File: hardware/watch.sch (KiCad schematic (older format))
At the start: 42 parts, among them J1 Conn_01x04_Male, J2 Conn_01x04_Male, SW1 SW_Push, SW2 SW_Push, U1 KCSA02-105, U10 STP08DP05, U11 KCSA02-105, U12 STP08DP05, U13 KCSA02-105, U2 KCSA02-105, U3 STP08DP05, U4 STP08DP05, U5 STM32L011F4Px, U6 TLV70033_SOT23-5, U7 MCP73831-2-OT, U8 LM66100, U9 LM66100, Y1 32kHz

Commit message: updated firmware
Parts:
- removed J1, J2: Conn_01x04_Male, watch:CONN_1x4_SMD, symbol Connector:Conn_01x04_Male
- added J1: Conn_01x02_Male, Connector_PinHeader_2.54mm:PinHeader_1x02_P2.54mm_Vertical, symbol Connector:Conn_01x02_Male
- added J2, J4: Conn_01x03_Male, Connector_PinHeader_2.54mm:PinHeader_1x03_P2.54mm_Vertical, symbol Connector:Conn_01x03_Male
- added J3, J5: Conn_01x01_Male, Connector_PinHeader_2.54mm:PinHeader_1x01_P2.54mm_Vertical, symbol Connector:Conn_01x01_Male
- BT1: footprint watch:BAT_PAD -> Connector_PinHeader_2.54mm:PinHeader_1x02_P2.54mm_Vertical
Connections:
- wire segments 134 -> 138
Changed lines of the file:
@@
 Title "Armbanduhr"
 Date "2020-09-20"
-Rev "1"
+Rev "2"
 Comp "Probieren geht über studieren. Immer."
 Comment1 "Andreas Kohler"
@@
 F 0 "BT1" H 2418 6146 50  0000 L CNN
 F 1 "Battery_Cell" H 2418 6055 50  0000 L CNN
-F 2 "watch:BAT_PAD" V 2300 6110 50  0001 C CNN
+F 2 "Connector_PinHeader_2.54mm:PinHeader_1x02_P2.54mm_Vertical" V 2300 6110 50  0001 C CNN
 F 3 "~" V 2300 6110 50  0001 C CNN
 F 4 "https://www.amazon.de/Turnigy-nano-tech-300mah-Solo-Pro-Modellbau/dp/B016339JKO/" H 2300 6050 50  0001 C CNN "Order"
@@
 	1    0    0    -1
 $EndComp
-$Comp
-L Connector:Conn_01x04_Male J1
-U 1 1 5F717493
-P 4300 950
-F 0 "J1" H 4408 1231 50  0000 C CNN
-F 1 "Conn_01x04_Male" H 4408 1140 50  0000 C CNN
-F 2 "watch:CONN_1x4_SMD" H 4300 950 50  0001 C CNN
-F 3 "~" H 4300 950 50  0001 C CNN
-F 4 "-" H 4300 950 50  0001 C CNN "Order"
-	1    4300 950
-	1    0    0    -1
-$EndComp
 Wire Wire Line
 	4500 1150 4750 1150
@@
 Wire Wire Line
 	4500 850  4750 850
-$Comp
-L Connector:Conn_01x04_Male J2
-U 1 1 5F7BC566
-P 5400 1050
-F 0 "J2" H 5508 1331 50  0000 C CNN
-F 1 "Conn_01x04_Male" H 5508 1240 50  0000 C CNN
-F 2 "watch:CONN_1x4_SMD" H 5400 1050 50  0001 C CNN
-F 3 "~" H 5400 1050 50  0001 C CNN
-F 4 "-" H 5400 1050 50  0001 C CNN "Order"
-	1    5400 1050
-	1    0    0    -1
-$EndComp
 Wire Wire Line
 	6000 1350 6000 1250
@@
 P 6000 1250
 F 0 "#FLG0103" H 6000 1325 50  0001 C CNN
-F 1 "PWR_FLAG" V 6000 1378 50  0000 L CNN
+F 1 "PWR_FLAG" V 6000 1378 50  0001 L CNN
 F 2 "" H 6000 1250 50  0001 C CNN
 F 3 "~" H 6000 1250 50  0001 C CNN
@@
 P 6000 950
 F 0 "#FLG0101" H 6000 1025 50  0001 C CNN
-F 1 "PWR_FLAG" H 6000 1123 50  0000 C CNN
+F 1 "PWR_FLAG" V 6000 1250 50  0001 C CNN
 F 2 "" H 6000 950 50  0001 C CNN
 F 3 "~" H 6000 950 50  0001 C CNN
 	1    6000 950
-	1    0    0    -1
-$EndComp
+	0    1    1    0
+$EndComp
+$Comp
+L Connector:Conn_01x01_Male J5
+U 1 1 5F7EF34B
+P 5400 1250
+F 0 "J5" H 5350 1250 50  0000 C CNN
+F 1 "Conn_01x01_Male" H 5508 1340 50  0001 C CNN
+F 2 "Connector_PinHeader_2.54mm:PinHeader_1x01_P2.54mm_Vertical" H 5400 1250 50  0001 C CNN
+F 3 "~" H 5400 1250 50  0001 C CNN
+	1    5400 1250
+	1    0    0    -1
+$EndComp
+$Comp
+L Connector:Conn_01x01_Male J3
+U 1 1 5F7FAF63
+P 4300 1150
+F 0 "J3" H 4250 1150 50  0000 C CNN
+F 1 "Conn_01x01_Male" H 4408 1240 50  0001 C CNN
+F 2 "Connector_PinHeader_2.54mm:PinHeader_1x01_P2.54mm_Vertical" H 4300 1150 50  0001 C CNN
+F 3 "~" H 4300 1150 50  0001 C CNN
+	1    4300 1150
+	1    0    0    -1
+$EndComp
+$Comp
+L Connector:Conn_01x03_Male J2
+U 1 1 5F80179E
+P 4300 950
+F 0 "J2" H 4250 1050 50  0000 C CNN
+F 1 "Conn_01x03_Male" H 4408 1140 50  0001 C CNN
+F 2 "Connector_PinHeader_2.54mm:PinHeader_1x03_P2.54mm_Vertical" H 4300 950 50  0001 C CNN
+F 3 "~" H 4300 950 50  0001 C CNN
+	1    4300 950
+	1    0    0    -1
+$EndComp
+$Comp
+L Connector:Conn_01x03_Male J4
+U 1 1 5F80247D
+P 5400 1050
+F 0 "J4" H 5350 1150 50  0000 C CNN
+F 1 "Conn_01x03_Male" H 5508 1240 50  0001 C CNN
+F 2 "Connector_PinHeader_2.54mm:PinHeader_1x03_P2.54mm_Vertical" H 5400 1050 50  0001 C CNN
+F 3 "~" H 5400 1050 50  0001 C CNN
+	1    5400 1050
+	1    0    0    -1
+$EndComp
+$Comp
+L Connector:Conn_01x02_Male J1
+U 1 1 5F812804
+P 2050 6850
+F 0 "J1" H 1950 6850 50  0000 C CNN
+F 1 "Conn_01x02_Male" H 2158 6940 50  0001 C CNN
+F 2 "Connector_PinHeader_2.54mm:PinHeader_1x02_P2.54mm_Vertical" H 2050 6850 50  0001 C CNN
+F 3 "~" H 2050 6850 50  0001 C CNN
+	1    2050 6850
+	1    0    0    -1
+$EndComp
+$Comp
+L power:GND #PWR0136
+U 1 1 5F8133F9
+P 2300 7000
+F 0 "#PWR0136" H 2300 6750 50  0001 C CNN
+F 1 "GND" H 2305 6827 50  0000 C CNN
+F 2 "" H 2300 7000 50  0001 C CNN
+F 3 "" H 2300 7000 50  0001 C CNN
+	1    2300 7000
+	1    0    0    -1
+$EndComp
+Wire Wire Line
+	2300 7000 2300 6950
+Wire Wire Line
+	2300 6950 2250 6950
+Wire Wire Line
+	2250 6850 2300 6850
+Wire Wire Line
+	2300 6850 2300 6950
+Connection ~ 2300 6950
 $EndSCHEMATC

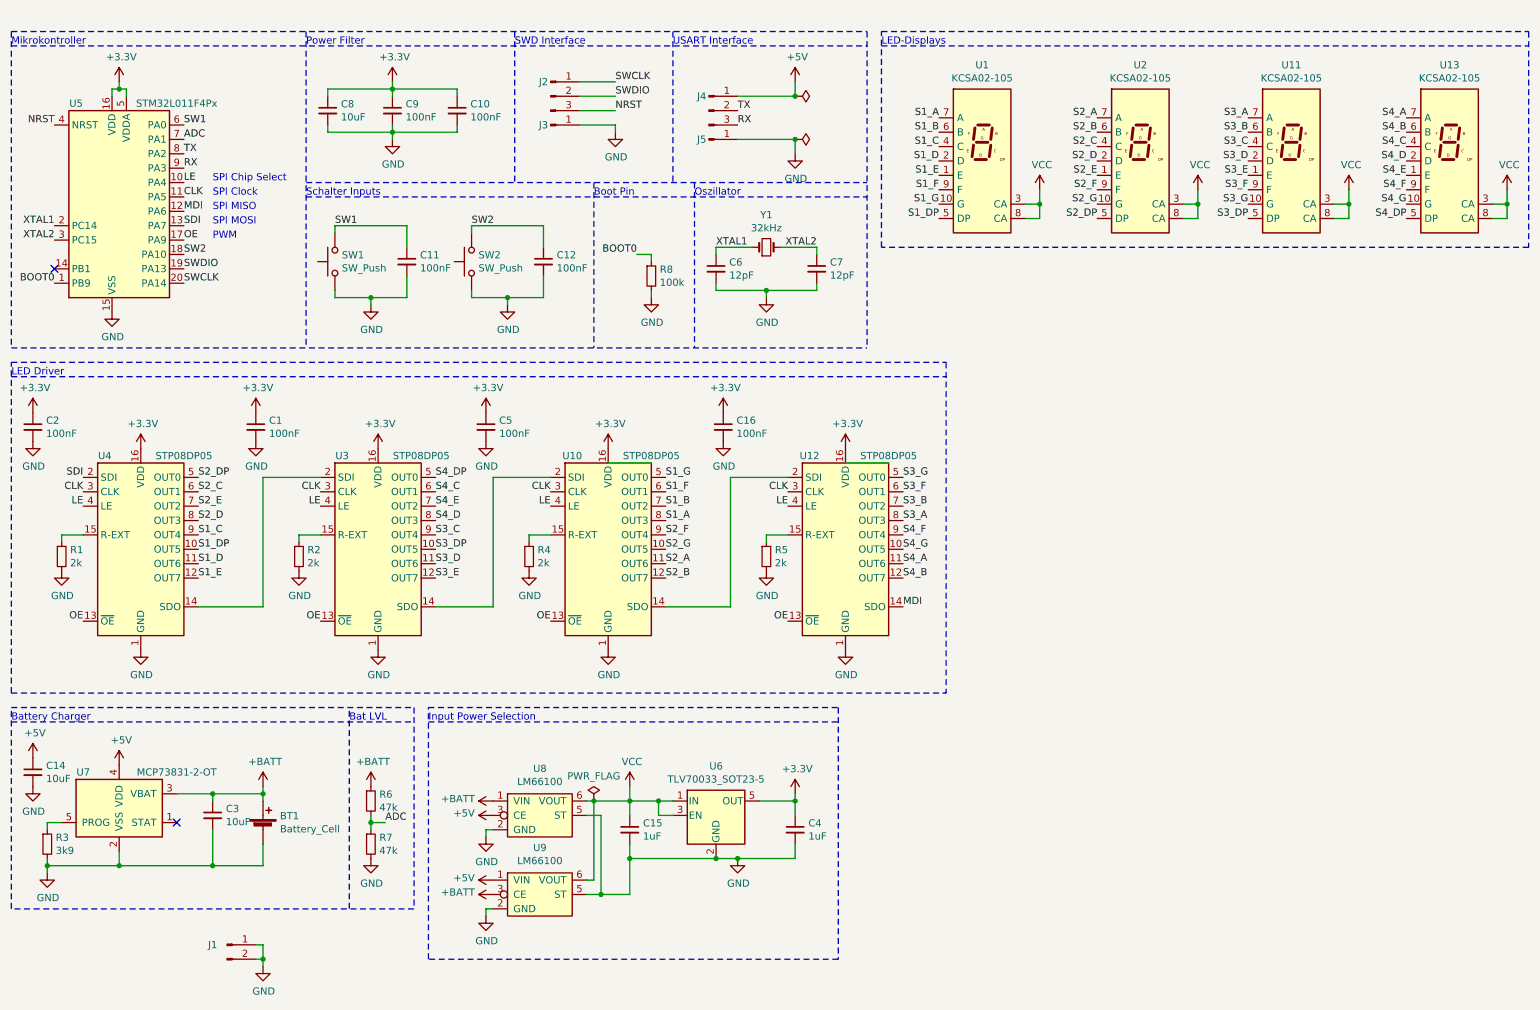
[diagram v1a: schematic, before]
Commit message: Hw3 (#4)
* working on hardware rev3

* fixed usb type c cc pin termination

* reverse current protection

* hardware development

* schematic should be done, pcb is next

* wip hw

* finished routing

* calc current consumption

* calculate current consumption

* added 3d models

* file cleanup

* added some vias to gnd plane

* added powerflags

* minor improvements

* updated schematic info

* more stitching vias

* added order references to parts

* modified bom

* Fixed outdated BOM Item

* Fixed two hardware issues.

Issue 1: Swapped USB D+/- lines
Issue 2: Wrong schematic smybol for power switch

* new case

* added svd file to repo

* fixed critical bug within reg::or_together

* fixed bug in bit_rs::set

* adapted display driver for hw3

* fixed rtc isr bug

* smaller button

* bigger case

* [fw] fixed rtc init bug

* [fw] fixed battery level bug
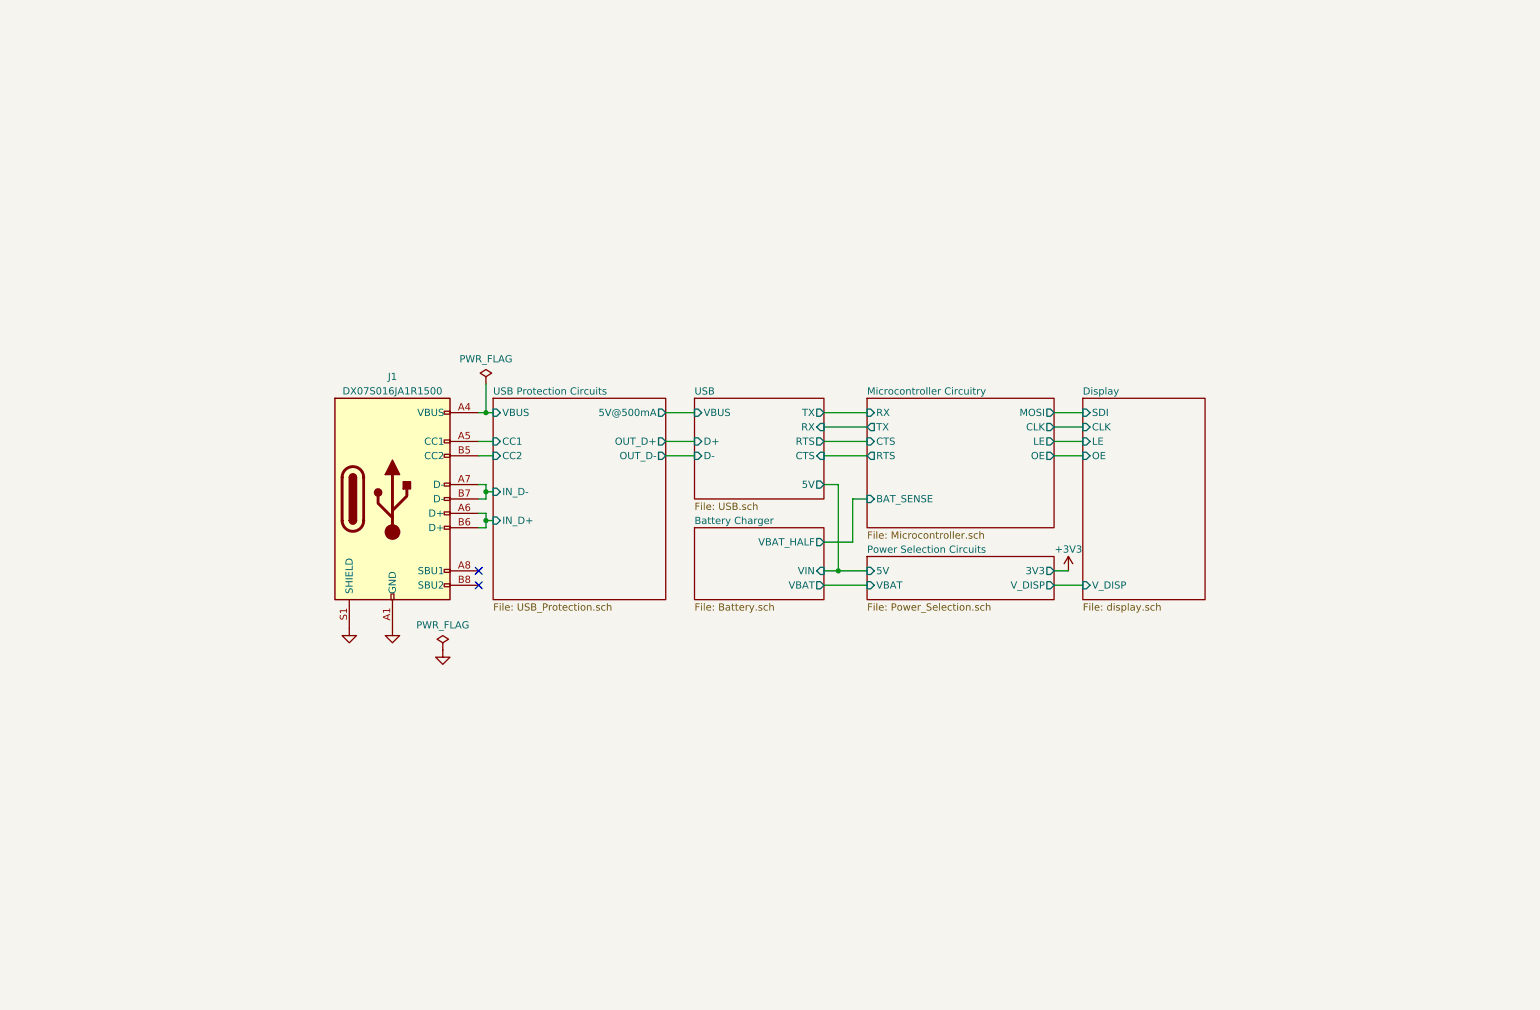
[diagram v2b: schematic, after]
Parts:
- removed BT1: Battery_Cell, Connector_PinHeader_2.54mm:PinHeader_1x02_P2.54mm_Vertical, symbol Device:Battery_Cell
- removed C1, C10, C11, C12, C16, C2, C5, C9: 100nF, Capacitor_SMD:C_0603_1608Metric_Pad1.05x0.95mm_HandSolder, symbol Device:C_Small
- removed C14, C3, C8: 10uF, Capacitor_SMD:C_0603_1608Metric_Pad1.05x0.95mm_HandSolder, symbol Device:C_Small
- removed C15, C4: 1uF, Capacitor_SMD:C_0603_1608Metric_Pad1.05x0.95mm_HandSolder, symbol Device:C_Small
- removed C6, C7: 12pF, Capacitor_SMD:C_0603_1608Metric_Pad1.05x0.95mm_HandSolder, symbol Device:C_Small
- removed J1: Conn_01x02_Male, Connector_PinHeader_2.54mm:PinHeader_1x02_P2.54mm_Vertical, symbol Connector:Conn_01x02_Male
- removed J2, J4: Conn_01x03_Male, Connector_PinHeader_2.54mm:PinHeader_1x03_P2.54mm_Vertical, symbol Connector:Conn_01x03_Male
- removed J3, J5: Conn_01x01_Male, Connector_PinHeader_2.54mm:PinHeader_1x01_P2.54mm_Vertical, symbol Connector:Conn_01x01_Male
- removed R1, R2, R4, R5: 2k, Resistor_SMD:R_0603_1608Metric_Pad1.05x0.95mm_HandSolder, symbol Device:R_Small
- removed R3: 3k9, Resistor_SMD:R_0603_1608Metric_Pad1.05x0.95mm_HandSolder, symbol Device:R_Small
- removed R6, R7: 47k, Resistor_SMD:R_0603_1608Metric_Pad1.05x0.95mm_HandSolder, symbol Device:R_Small
- removed R8: 100k, Resistor_SMD:R_0603_1608Metric_Pad1.05x0.95mm_HandSolder, symbol Device:R_Small
- removed SW1, SW2: SW_Push, Button_Switch_SMD:SW_Push_1P1T_NO_CK_KMR2, symbol Switch:SW_Push
- removed U1, U11, U13, U2: KCSA02-105, Display_7Segment:KCSC02-105, symbol Display_Character:KCSA02-105
- removed U10, U12, U3, U4: STP08DP05, Package_SO:TSSOP-16_4.4x5mm_P0.65mm, symbol Driver_LED:STP08CP05
- removed U5: STM32L011F4Px, Package_SO:TSSOP-20_4.4x6.5mm_P0.65mm, symbol MCU_ST_STM32L0:STM32L011F4Px
- removed U6: TLV70033_SOT23-5, Package_TO_SOT_SMD:SOT-23-5, symbol Regulator_Linear:TLV70033_SOT23-5
- removed U7: MCP73831-2-OT, Package_TO_SOT_SMD:SOT-23-5, symbol Battery_Management:MCP73831-2-OT
- removed U8, U9: LM66100, lm66100:LM66100DCKT, symbol watch:LM66100
- removed Y1: 32kHz, Crystal:Crystal_SMD_3215-2Pin_3.2x1.5mm, symbol Device:Crystal_Small
- added J1: DX07S016JA1R1500, watch:DX07S016JA1R1500, symbol Connector:USB_C_Receptacle_USB2.0
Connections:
- net labels added: +3V3
- net labels removed: +3.3V, +5V, +BATT, ADC, BOOT0, CLK, LE, MDI, NRST, OE, RX, S1_A, S1_B, S1_C, S1_D, S1_DP, S1_E, S1_F, S1_G, S2_A, S2_B, S2_C, S2_D, S2_DP, S2_E, S2_F, S2_G, S3_A, S3_B, S3_C, S3_D, S3_DP, S3_E, S3_F, S3_G, S4_A, S4_B, S4_C, S4_D, S4_DP, S4_E, S4_F, S4_G, SDI, SW1, SW2, SWCLK, SWDIO, TX, VCC, XTAL1, XTAL2
- wire segments 138 -> 36
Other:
- note removed: "Bat LVL"
- note removed: "Battery Charger"
- note removed: "Boot Pin"
- note removed: "Input Power Selection"
- note removed: "LED Driver"
- note removed: "LED-Displays"
- note removed: "Mikrokontroller"
- note removed: "Oszillator"
- note removed: "PWM"
- note removed: "Power Filter"
- note removed: "SPI Chip Select"
- note removed: "SPI Clock"
- note removed: "SPI MISO"
- note removed: "SPI MOSI"
- note removed: "SWD Interface"
- note removed: "Schalter Inputs"
- note removed: "USART Interface"
